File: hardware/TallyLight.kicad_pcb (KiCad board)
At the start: 4 copper layers, 68 x 68 mm, 179 parts, among them J1 Hanrun HY931147C, J2 USB_C_Receptacle_USB2.0, J3 Strapping, SW1 SW_Push, T2 HR051067, U10 EL357N(B)(TA)-G, U11 CJ431, U2 KSZ8851SNL, U3 SRV05-4, U4 ESP32-C3-WROOM-02, U5 AMS1117-3.3, U7 SRV05-4, U9 Si3402-B, Y1 25MHz

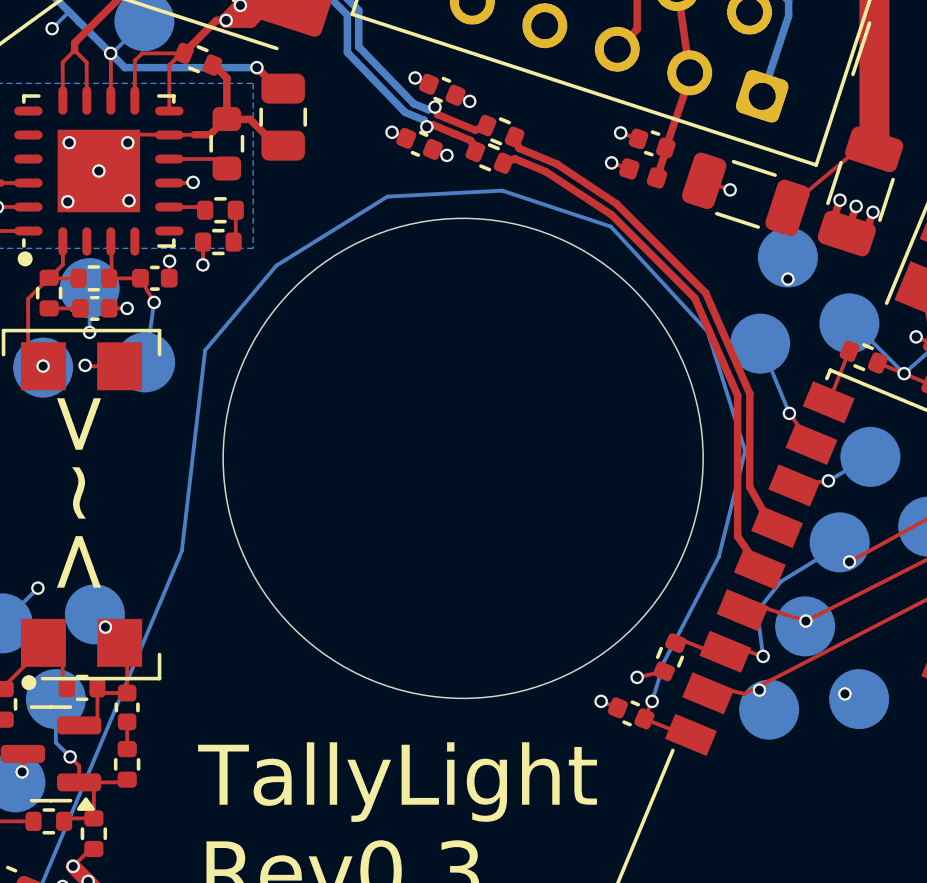
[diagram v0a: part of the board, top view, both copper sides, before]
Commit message: Make button trace around center hole more round
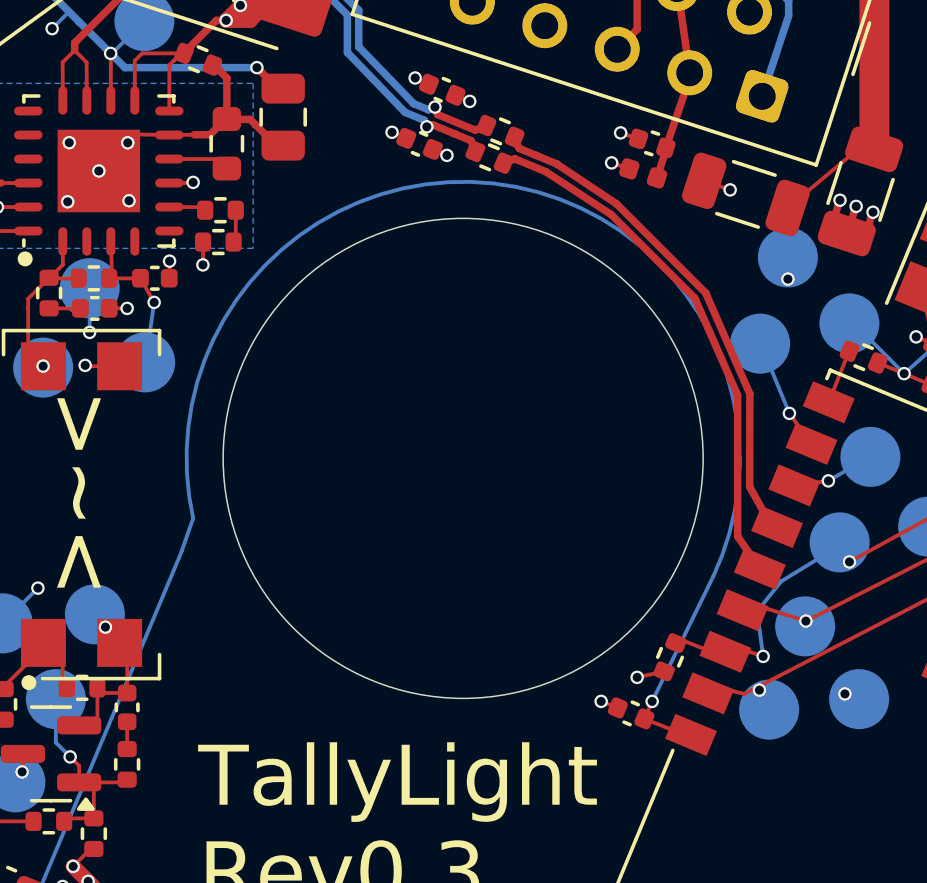
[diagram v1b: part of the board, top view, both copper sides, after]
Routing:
- net /Logic/BUTTON: track 66.5 -> 32.0 mm
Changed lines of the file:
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@@
 		)
 	)
+	(gr_arc
+		(start 141 102)
+		(mid 151.017482 90.836773)
+		(end 158.342016 103.925655)
+		(stroke
+			(width 0.127)
+			(type default)
+		)
+		(layer "B.Cu")
+		(net 15)
+	)
 	(gr_circle
 		(center 150 100)
@@
 	)
 	(segment
-		(start 151.3 91.075)
-		(end 154.925 92.275)
-		(width 0.127)
-		(layer "B.Cu")
-		(net 15)
-	)
-	(segment
-		(start 158.525 103.275)
-		(end 159.4 99.75)
-		(width 0.127)
-		(layer "B.Cu")
-		(net 15)
-	)
-	(segment
-		(start 154.925 92.275)
-		(end 158.15 95.775)
-		(width 0.127)
-		(layer "B.Cu")
-		(net 15)
-	)
-	(segment
-		(start 156.7 106.775)
-		(end 158.525 103.275)
-		(width 0.127)
-		(layer "B.Cu")
-		(net 15)
-	)
-	(segment
-		(start 156.3 108.1)
-		(end 156.7 106.775)
-		(width 0.127)
-		(layer "B.Cu")
-		(net 15)
-	)
-	(segment
-		(start 158.15 95.775)
-		(end 159.4 99.75)
-		(width 0.127)
-		(layer "B.Cu")
-		(net 15)
-	)
-	(segment
 		(start 140.525 103.325)
 		(end 140.625 103.075)
@@
 	)
 	(segment
-		(start 141.4 96.4)
-		(end 143.775 93.575)
-		(width 0.127)
-		(layer "B.Cu")
-		(net 15)
-	)
-	(segment
-		(start 140.625 103.075)
-		(end 141.4 96.4)
-		(width 0.127)
-		(layer "B.Cu")
-		(net 15)
-	)
-	(segment
-		(start 147.475 91.275)
-		(end 151.3 91.075)
+		(start 158.342016 103.925655)
+		(end 156.3 108.1)
 		(width 0.127)
 		(layer "B.Cu")
@@
 	)
 	(segment
-		(start 143.775 93.575)
-		(end 147.475 91.275)
+		(start 132.75 121.825)
+		(end 140.525 103.325)
 		(width 0.127)
 		(layer "B.Cu")
@@
 	)
 	(segment
-		(start 132.75 121.825)
-		(end 140.525 103.325)
+		(start 141 102)
+		(end 140.625 103.075)
 		(width 0.127)
 		(layer "B.Cu")
